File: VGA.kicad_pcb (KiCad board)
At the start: 2 copper layers, 115.6 x 99.7 mm, 47 parts, among them J1 DB15_Female_HighDensity_Mount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, J2 Conn_02x20_Odd_Even, J3 Conn_02x20_Odd_Even, SW1 SW_DIP_x03, U1 74HC04, U10 TC551001, U11 SST39SF010A, U12 74HC244, U13 74HC244, U14 74HC02, U15 74HC244, U16 74LS245, U2 74HC74, U3 CD74HC08, U4 4040, U5 74HC273, U6 SST39SF010A, U7 4040, U8 74LS195, U9 74LS195, Y1 25M

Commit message: 信号生成部設計完了
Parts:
- added C1: C, Capacitor_THT:C_Disc_D7.0mm_W2.5mm_P5.00mm, F.Cu at (151.1, 113.1)
- added G***: LOGO, LOGO, F.Cu at (153.7, 48.9)
- added H1: MountingHole_Pad, MountingHole:MountingHole_3mm_Pad, F.Cu at (73.7, 137.8)
- added H2: MountingHole_Pad, MountingHole:MountingHole_3mm_Pad, F.Cu at (73.7, 48.3)
- added H3: MountingHole_Pad, MountingHole:MountingHole_3mm_Pad, F.Cu at (181.0, 137.8)
- added H4: MountingHole_Pad, MountingHole:MountingHole_3mm_Pad, F.Cu at (181.0, 48.3)
- moved C14 67.4 mm to (115.6, 55.9)
- moved C3 63.9 mm to (119.4, 123.2)
- moved C4 58.4 mm to (86.4, 68.6)
- moved C10 53.5 mm to (125.7, 111.8)
- moved C12 49.8 mm to (81.3, 105.5)
- moved C8 38.4 mm to (114.9, 68.6)
- moved C5 35.5 mm to (144.8, 68.6)
- moved C6 33.3 mm to (151.1, 103.5)
- moved C13 29.2 mm to (86.4, 55.9)
- moved C9 26.9 mm to (125.7, 104.1)
- moved C11 23.5 mm to (81.3, 81.9)
- moved C7 17.2 mm to (125.7, 81.9)
- moved J1 3.54 mm to (75.7, 73.3)
- moved R5 3.54 mm to (80.4, 73.3)
- moved R6 3.54 mm to (80.4, 70.8)
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- renumbered C1 to C19, U9 to U10, U10 to U11, U11 to U12, U12 to U13, U13 to U14, U14 to U3, U3 to U4, U4 to U5, U5 to U6, U6 to U7, U7 to U8, U8 to U9
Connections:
- U13 pad 17: unconnected-(U12-Pad17) -> GND
- U13 pad 2: unconnected-(U12-Pad2) -> GND
- U3 pad 12: Net-(U14-Pad12) -> ~{WE}
- U3 pad 2: Net-(U14-Pad12) -> Net-(U3-Pad2)
- U3 pad 3: Net-(U14-Pad12) -> Net-(U3-Pad2)
- U3 pad 4: Net-(U14-Pad12) -> Net-(U3-Pad2)
- U7 pad 2: unconnected-(U6-Pad2) (its old number) -> GND
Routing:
- net ~{WE}: track 79.1 -> 96.7 mm
- net Net-(U14-Pad12): track 12.7 -> 0.00 mm
- net VCC: track 570.8 -> 579.1 mm
- net CRAM_Addr2: track 119.4 -> 125.7 mm
- net CRAM_Addr1: track 115.8 -> 122.1 mm
- net CRAM_Addr0: track 110.7 -> 117.0 mm
- net CRAM_Addr3: track 132.4 -> 137.9 mm
- net B: track 43.7 -> 49.1 mm
- net Net-(U3-Pad2): track 0.00 -> 5.08 mm
- net G: track 34.6 -> 39.5 mm
- net R: track 28.1 -> 32.9 mm
- net GND: track 391.3 -> 395.3 mm, vias 20 -> 125
- net V_Sync: track 143.1 -> 146.5 mm
- net H_Sync: track 128.7 -> 132.1 mm
- net V_Addr9: track 37.2 -> 34.6 mm
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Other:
- board size 115.6 x 99.7 mm -> 117.5 x 99.7 mm
- board text added: "25MHz"
- board text added: "> M58725"
- board text added: "Address MUX"
- board text added: "Bus ctrl"
- board text added: "Bus transceiver"
- board text added: "CG ROM"
- board text added: "Clock generator"
- board text added: "H Counter"
- board text added: "M57825"
- board text added: "NLP-16A v1.0 VGA video Module"
- board text added: "R G B"
- board text added: "System ROM"
- board text added: "TC551001"
- board text added: "Text VRAM"
- board text added: "Timing generator"
- board text added: "V Counter"
- board text added: "video signal generator"

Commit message: 完成版
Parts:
- added D1: LED, LED_THT:LED_D3.0mm, F.Cu at (74.3, 131.4)
- added D2: LED, LED_THT:LED_D3.0mm, F.Cu at (74.3, 122.6)
- added D3: LED, LED_THT:LED_D3.0mm, F.Cu at (74.3, 127.0)
- added R10: R, Resistor_SMD:R_0603_1608Metric_Pad0.98x0.95mm_HandSolder, F.Cu at (76.8, 126.1)
- added R8: R, Resistor_SMD:R_0603_1608Metric_Pad0.98x0.95mm_HandSolder, F.Cu at (76.8, 130.5)
- added R9: R, Resistor_SMD:R_0603_1608Metric_Pad0.98x0.95mm_HandSolder, F.Cu at (76.8, 121.6)
- added RN1: R_Network04, Resistor_THT:R_Array_SIP5, F.Cu at (79.4, 135.9)
- added SW2: SW_DIP_x04, Button_Switch_THT:SW_DIP_SPSTx04_Piano_10.8x11.72mm_W7.62mm_P2.54mm, F.Cu at (70.5, 109.2)
- added TP1: TestPoint, TestPoint:TestPoint_THTPad_D1.0mm_Drill0.5mm, F.Cu at (182.2, 99.7)
- added TP2: TestPoint, TestPoint:TestPoint_THTPad_D1.0mm_Drill0.5mm, F.Cu at (182.2, 102.9)
- added TP3: TestPoint, TestPoint:TestPoint_THTPad_D1.0mm_Drill0.5mm, F.Cu at (182.2, 106.0)
- JP1: footprint Jumper:SolderJumper-3_P1.3mm_Bridged12_Pad1.0x1.5mm -> Jumper:SolderJumper-3_P1.3mm_Open_RoundedPad1.0x1.5mm
- SW1: footprint Button_Switch_THT:SW_DIP_SPSTx03_Slide_9.78x9.8mm_W7.62mm_P2.54mm -> Button_Switch_THT:SW_DIP_SPSTx03_Piano_10.8x9.18mm_W7.62mm_P2.54mm
- moved C19 105.6 mm to (144.1, 136.6), turned to -90 degrees
- moved R3 1.27 mm to (82.2, 99.7)
- moved R4 1.27 mm to (82.2, 102.2)
- moved SW1 0.59 mm to (70.5, 97.2)
- moved R2 0.36 mm to (81.3, 97.2), turned to 90 degrees
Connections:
- J3 pad 37: VCC -> unconnected-(J3-Pad37)
- J3 pad 39: VCC -> unconnected-(J3-Pad39)
- U11 pad 28: GND -> VCC
- U12 pad 25: GND -> F_mode0
- U12 pad 28: GND -> F_mode2
- U12 pad 29: GND -> F_mode3
- U12 pad 4: GND -> F_mode1
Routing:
- net F_mode3: track 0.00 -> 43.4 mm
- net F_mode0: track 0.00 -> 42.5 mm
- net F_mode2: track 0.00 -> 41.9 mm
- net F_mode1: track 0.00 -> 37.4 mm, vias 0 -> 1
- net VCC: track 579.1 -> 615.5 mm
- net Visible: track 122.6 -> 143.4 mm
- net ~{WE}: track 96.7 -> 116.7 mm
- net ~{OE}: track 100.9 -> 119.8 mm
- net V_Sync: track 146.5 -> 156.0 mm
- net H_Sync: track 132.1 -> 141.4 mm
- net GND: track 395.3 -> 387.7 mm, vias 125 -> 175
- net Net-(D2-Pad1): track 0.00 -> 2.54 mm
- net Net-(D1-Pad1): track 0.00 -> 2.54 mm
- net Net-(D3-Pad1): track 0.00 -> 2.53 mm
- net R: track 32.9 -> 31.3 mm
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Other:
- board text added: "02"
- board text added: "04"
- board text added: "08"
- board text added: "195"
- board text added: "244"
- board text added: "245"
- board text added: "273"
- board text added: "4040"
- board text added: "74"
- board text added: "Color R G B"
- board text added: "Font"
- board text added: "HS"
- board text added: "PWR"
- board text added: "RD"
- board text added: "SST39SF010"
- board text added: "VS"
- board text added: "Visi"
- board text added: "WR"
- board text removed: "R G B"

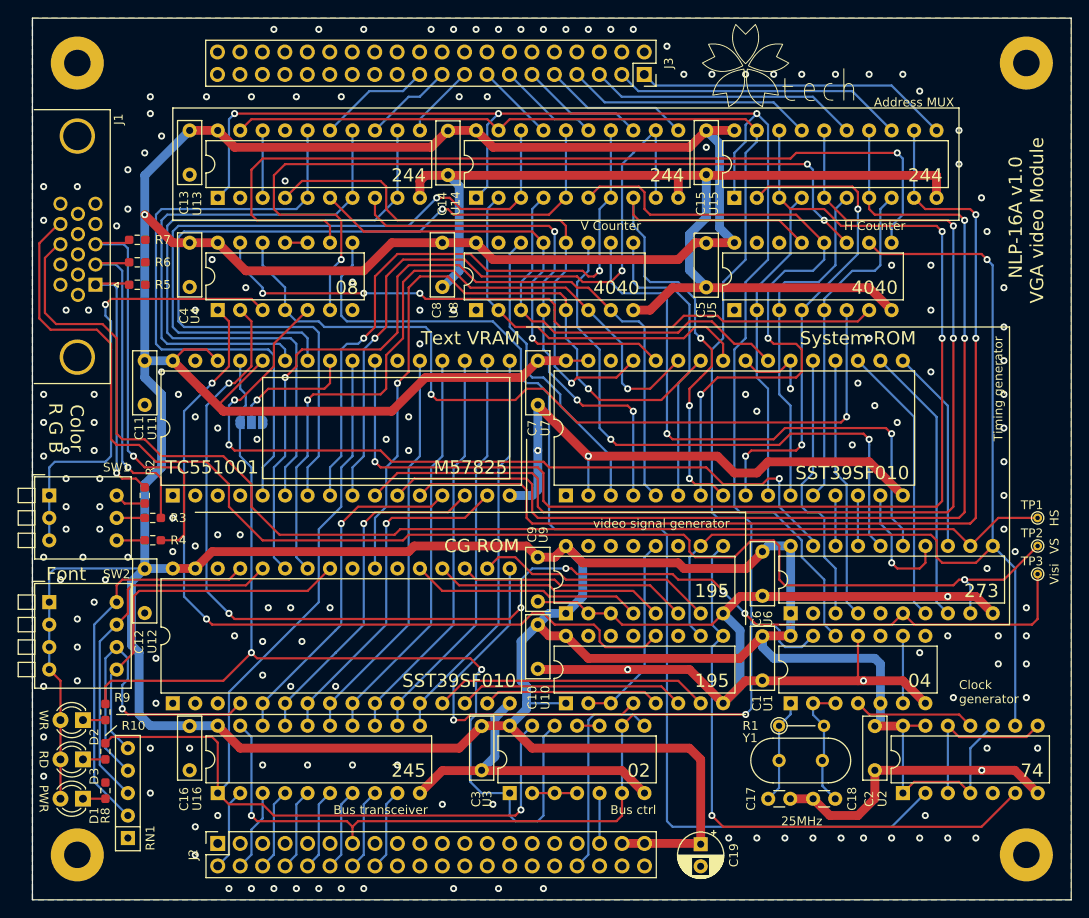
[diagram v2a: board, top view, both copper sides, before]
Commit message: 電源ライン増強他
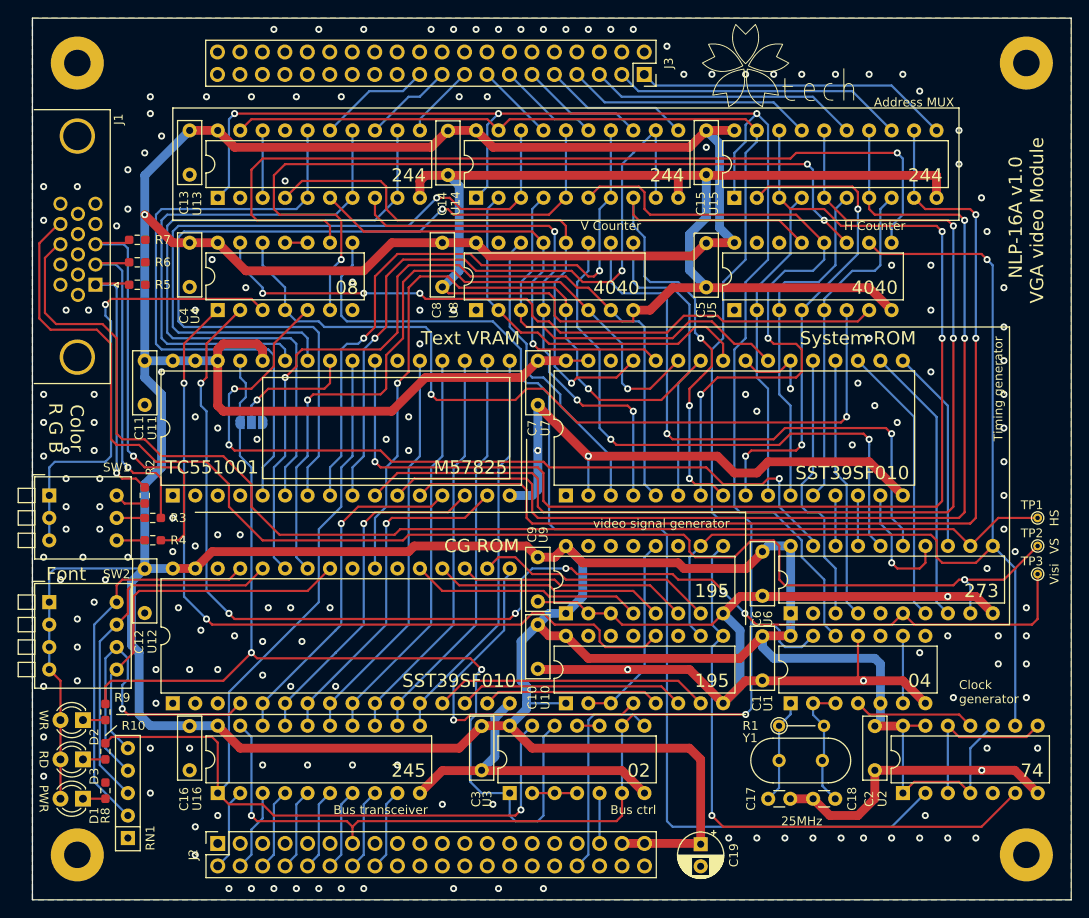
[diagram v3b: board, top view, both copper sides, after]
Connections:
- U11 pad 31: GND -> VCC
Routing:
- net GND: track 387.7 -> 413.3 mm, vias 175 -> 178
- net VCC: track 615.5 -> 613.0 mm
- net V_Addr4: track 45.1 -> 46.4 mm
- net Net-(U10-Pad12): track 93.1 -> 92.0 mm
- net Visible: track 143.4 -> 142.5 mm
- net H_COUNT_RS: track 92.8 -> 93.6 mm
- net V_Addr5: track 43.7 -> 44.2 mm

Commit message: 内部バスプルアップ追加他/基板製造バージョン
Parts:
- added R11: R, Resistor_SMD:R_0603_1608Metric_Pad0.98x0.95mm_HandSolder, B.Cu at (94.6, 126.4)
- added R12: R, Resistor_SMD:R_0603_1608Metric_Pad0.98x0.95mm_HandSolder, B.Cu at (97.2, 126.4)
- added R13: R, Resistor_SMD:R_0603_1608Metric_Pad0.98x0.95mm_HandSolder, B.Cu at (99.7, 126.4)
- added R14: R, Resistor_SMD:R_0603_1608Metric_Pad0.98x0.95mm_HandSolder, B.Cu at (102.2, 126.4)
- added R15: R, Resistor_SMD:R_0603_1608Metric_Pad0.98x0.95mm_HandSolder, B.Cu at (104.8, 126.4)
- added R16: R, Resistor_SMD:R_0603_1608Metric_Pad0.98x0.95mm_HandSolder, B.Cu at (107.3, 126.4)
- added R17: R, Resistor_SMD:R_0603_1608Metric_Pad0.98x0.95mm_HandSolder, B.Cu at (109.9, 126.4)
- added R18: R, Resistor_SMD:R_0603_1608Metric_Pad0.98x0.95mm_HandSolder, B.Cu at (112.4, 126.4)
- moved C19 105.6 mm to (84.5, 49.5), turned to 90 degrees
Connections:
- J2 pad 37: VCC -> unconnected-(J2-Pad37)
- J2 pad 39: VCC -> unconnected-(J2-Pad39)
- J3 pad 37: unconnected-(J3-Pad37) -> VCC
- J3 pad 39: unconnected-(J3-Pad39) -> VCC
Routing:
- net VCC: track 613.0 -> 606.9 mm, vias 1 -> 2
- net C_DATA7: track 45.5 -> 47.7 mm
- net C_DATA6: track 45.5 -> 47.7 mm
- net C_DATA5: track 45.5 -> 47.7 mm
- net C_DATA4: track 45.5 -> 47.7 mm
- net C_DATA3: track 45.5 -> 47.7 mm
- net C_DATA2: track 39.3 -> 41.6 mm
- net C_DATA1: track 39.3 -> 41.6 mm
- net C_DATA0: track 39.3 -> 41.6 mm
- net GND: vias 178 -> 179

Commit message: VGAの入出力インターフェイス修正
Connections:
- U3 pad 12: ~{WE} -> ~{DE}
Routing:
- net ~{WE}: track 116.7 -> 99.2 mm
- net ~{DE}: track 222.1 -> 233.5 mm, vias 2 -> 3
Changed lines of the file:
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@@
       (net 165 "Net-(U3-Pad10)") (pintype "input"))
     (pad "12" thru_hole oval (at 7.62 5.08 90) (size 1.6 1.6) (drill 0.8) (layers *.Cu *.Mask)
-      (net 91 "~{WE}") (pintype "input"))
+      (net 31 "~{DE}") (pintype "input"))
     (pad "13" thru_hole oval (at 7.62 2.54 90) (size 1.6 1.6) (drill 0.8) (layers *.Cu *.Mask)
       (net 156 "~{OE}") (pintype "output"))
@@
   (segment (start 104.775 130.81) (end 103.505 132.08) (width 0.25) (layer "B.Cu") (net 30))
   (segment (start 103.505 137.775) (end 102.235 139.045) (width 0.25) (layer "B.Cu") (net 30))
+  (segment (start 128.905 133.985) (end 134.62 133.985) (width 0.25) (layer "F.Cu") (net 31))
   (segment (start 149.225 54.61) (end 150.495 55.88) (width 0.25) (layer "F.Cu") (net 31))
   (segment (start 93.345 54.61) (end 120.03 54.61) (width 0.25) (layer "F.Cu") (net 31))
@@
   (segment (start 92.075 55.88) (end 93.345 54.61) (width 0.25) (layer "F.Cu") (net 31))
   (segment (start 93.98 133.985) (end 104.14 133.985) (width 0.25) (layer "F.Cu") (net 31))
+  (segment (start 105.41 133.985) (end 128.905 133.985) (width 0.25) (layer "F.Cu") (net 31))
   (segment (start 104.14 133.985) (end 104.775 134.62) (width 0.25) (layer "F.Cu") (net 31))
   (segment (start 104.775 134.62) (end 105.41 133.985) (width 0.25) (layer "F.Cu") (net 31))
@@
   (segment (start 135.25 133.345) (end 135.25 130.81) (width 0.25) (layer "F.Cu") (net 31))
   (segment (start 136.52 121.92) (end 135.25 123.19) (width 0.25) (layer "F.Cu") (net 31))
-  (segment (start 105.41 133.985) (end 134.62 133.985) (width 0.25) (layer "F.Cu") (net 31))
+  (via (at 128.905 133.985) (size 0.8) (drill 0.4) (layers "F.Cu" "B.Cu") (net 31))
   (via (at 149.235 121.92) (size 0.8) (drill 0.4) (layers "F.Cu" "B.Cu") (net 31))
   (via (at 93.345 133.35) (size 0.8) (drill 0.4) (layers "F.Cu" "B.Cu") (net 31))
+  (segment (start 128.905 124.46) (end 128.905 133.985) (width 0.25) (layer "B.Cu") (net 31))
+  (segment (start 127.63 123.19) (end 128.9 124.46) (width 0.25) (layer "B.Cu") (net 31))
   (segment (start 149.225 99.695) (end 149.86 100.33) (width 0.25) (layer "B.Cu") (net 31))
   (segment (start 149.87 100.33) (end 149.87 111.76) (width 0.25) (layer "B.Cu") (net 31))
@@
   (segment (start 93.345 133.35) (end 93.345 124.46) (width 0.25) (layer "B.Cu") (net 31))
   (segment (start 149.225 58.42) (end 149.225 70.485) (width 0.25) (layer "B.Cu") (net 31))
+  (segment (start 128.9 124.46) (end 128.905 124.46) (width 0.25) (layer "B.Cu") (net 31))
   (segment (start 149.87 121.285) (end 149.87 114.3) (width 0.25) (layer "B.Cu") (net 31))
   (segment (start 146.05 99.695) (end 149.225 99.695) (width 0.25) (layer "B.Cu") (net 31))
@@
   (via (at 119.38 116.84) (size 0.8) (drill 0.4) (layers "F.Cu" "B.Cu") (net 91))
   (via (at 93.345 114.935) (size 0.8) (drill 0.4) (layers "F.Cu" "B.Cu") (net 91))
-  (segment (start 123.19 133.985) (end 125.73 133.985) (width 0.25) (layer "B.Cu") (net 91))
   (segment (start 93.345 93.98) (end 93.345 114.935) (width 0.25) (layer "B.Cu") (net 91))
   (segment (start 92.075 83.82) (end 92.71 84.455) (width 0.25) (layer "B.Cu") (net 91))
@@
   (segment (start 118.11 129.54) (end 119.38 130.81) (width 0.25) (layer "B.Cu") (net 91))
   (segment (start 92.075 81.92) (end 92.075 83.82) (width 0.25) (layer "B.Cu") (net 91))
-  (segment (start 125.73 133.985) (end 126.365 133.35) (width 0.25) (layer "B.Cu") (net 91))
-  (segment (start 126.365 133.35) (end 126.365 124.455) (width 0.25) (layer "B.Cu") (net 91))
   (segment (start 92.045 92.68) (end 93.345 93.98) (width 0.25) (layer "B.Cu") (net 91))
-  (segment (start 122.55 130.81) (end 122.55 133.345) (width 0.25) (layer "B.Cu") (net 91))
   (segment (start 92.045 86.7075) (end 92.045 88.9) (width 0.25) (layer "B.Cu") (net 91))
   (segment (start 118.745 117.475) (end 118.745 121.92) (width 0.25) (layer "B.Cu") (net 91))
@@
   (segment (start 119.38 116.84) (end 118.745 117.475) (width 0.25) (layer "B.Cu") (net 91))
   (segment (start 118.745 121.92) (end 118.11 122.555) (width 0.25) (layer "B.Cu") (net 91))
-  (segment (start 126.365 124.455) (end 127.63 123.19) (width 0.25) (layer "B.Cu") (net 91))
-  (segment (start 122.55 133.345) (end 123.19 133.985) (width 0.25) (layer "B.Cu") (net 91))
   (segment (start 118.11 122.555) (end 118.11 129.54) (width 0.25) (layer "B.Cu") (net 91))
   (segment (start 93.98 86.36) (end 95.25 85.09) (width 0.25) (layer "F.Cu") (net 92))

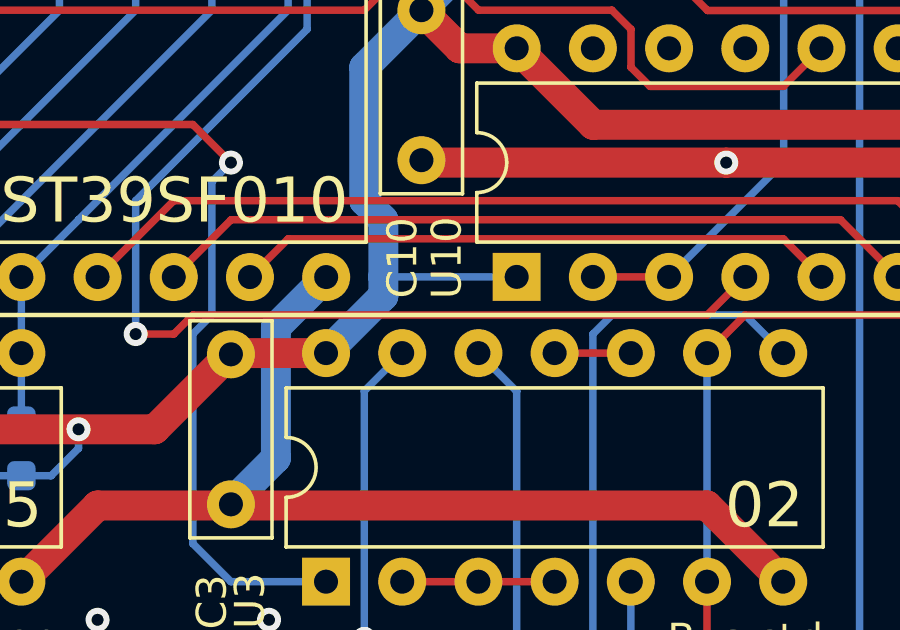
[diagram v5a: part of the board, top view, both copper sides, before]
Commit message: VRAMアクセス中の出力イネーブルを追加
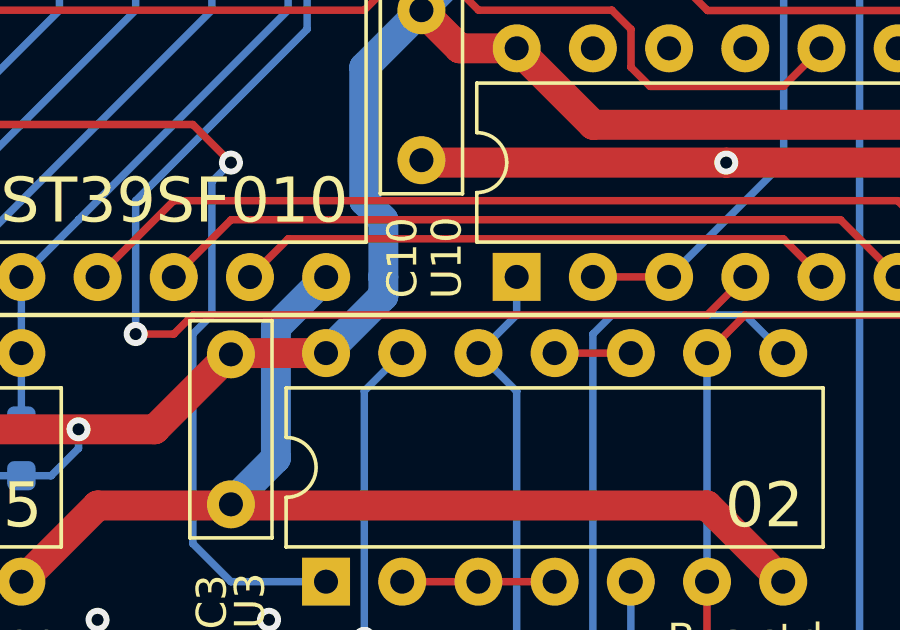
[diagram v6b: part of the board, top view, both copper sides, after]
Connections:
- U10 pad 1: VCC -> ~{DE}
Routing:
- net VCC: track 606.9 -> 602.4 mm
- net ~{DE}: track 233.5 -> 236.5 mm
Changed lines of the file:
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@@
     (fp_line (start 0.635 19.05) (end 0.635 -0.27) (layer "F.Fab") (width 0.1))
     (pad "1" thru_hole rect (at 0 0 90) (size 1.6 1.6) (drill 0.8) (layers *.Cu *.Mask)
-      (net 1 "VCC") (pinfunction "~{MR}") (pintype "input"))
+      (net 31 "~{DE}") (pinfunction "~{MR}") (pintype "input"))
     (pad "2" thru_hole oval (at 0 2.54 90) (size 1.6 1.6) (drill 0.8) (layers *.Cu *.Mask)
       (net 169 "Net-(U10-Pad2)") (pinfunction "J") (pintype "input"))
@@
   (segment (start 128.905 102.87) (end 130.81 104.775) (width 1) (layer "B.Cu") (net 1))
   (segment (start 151.14 113.11) (end 151.14 114.3) (width 1) (layer "B.Cu") (net 1))
-  (segment (start 128.905 120.65) (end 124.46 120.65) (width 0.25) (layer "B.Cu") (net 1))
   (segment (start 144.78 55.88) (end 146.28 57.38) (width 1) (layer "B.Cu") (net 1))
   (segment (start 80.645 121.92) (end 80.645 114.935) (width 1) (layer "B.Cu") (net 1))
@@
   (segment (start 127.63 123.19) (end 128.9 124.46) (width 0.25) (layer "B.Cu") (net 31))
   (segment (start 149.225 99.695) (end 149.86 100.33) (width 0.25) (layer "B.Cu") (net 31))
+  (segment (start 127.63 123.19) (end 128.9 121.92) (width 0.25) (layer "B.Cu") (net 31))
   (segment (start 149.87 100.33) (end 149.87 111.76) (width 0.25) (layer "B.Cu") (net 31))
   (segment (start 145.415 80.645) (end 145.415 99.06) (width 0.25) (layer "B.Cu") (net 31))
@@
   (segment (start 128.9 124.46) (end 128.905 124.46) (width 0.25) (layer "B.Cu") (net 31))
   (segment (start 149.87 121.285) (end 149.87 114.3) (width 0.25) (layer "B.Cu") (net 31))
+  (segment (start 128.9 121.92) (end 128.905 121.92) (width 0.25) (layer "B.Cu") (net 31))
   (segment (start 146.05 99.695) (end 149.225 99.695) (width 0.25) (layer "B.Cu") (net 31))
   (segment (start 149.235 121.92) (end 149.87 121.285) (width 0.25) (layer "B.Cu") (net 31))
+  (segment (start 128.905 121.92) (end 128.905 120.65) (width 0.25) (layer "B.Cu") (net 31))
   (segment (start 153.68 114.3) (end 153.045 113.665) (width 0.25) (layer "B.Cu") (net 31))
   (segment (start 153.045 113.665) (end 153.045 112.395) (width 0.25) (layer "B.Cu") (net 31))
